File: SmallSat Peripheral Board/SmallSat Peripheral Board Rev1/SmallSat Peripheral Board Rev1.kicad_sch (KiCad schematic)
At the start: 9 parts

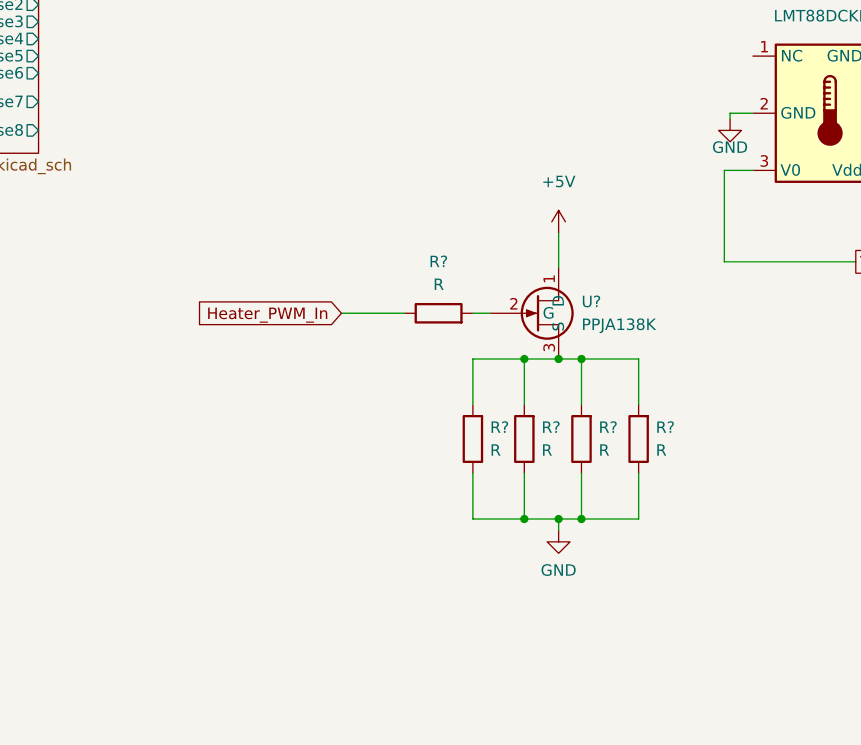
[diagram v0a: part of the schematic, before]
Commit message: Updated Power Section
Now using BQ28Z620DRZR fuel gauge
Now using BQ296202DSGR protection
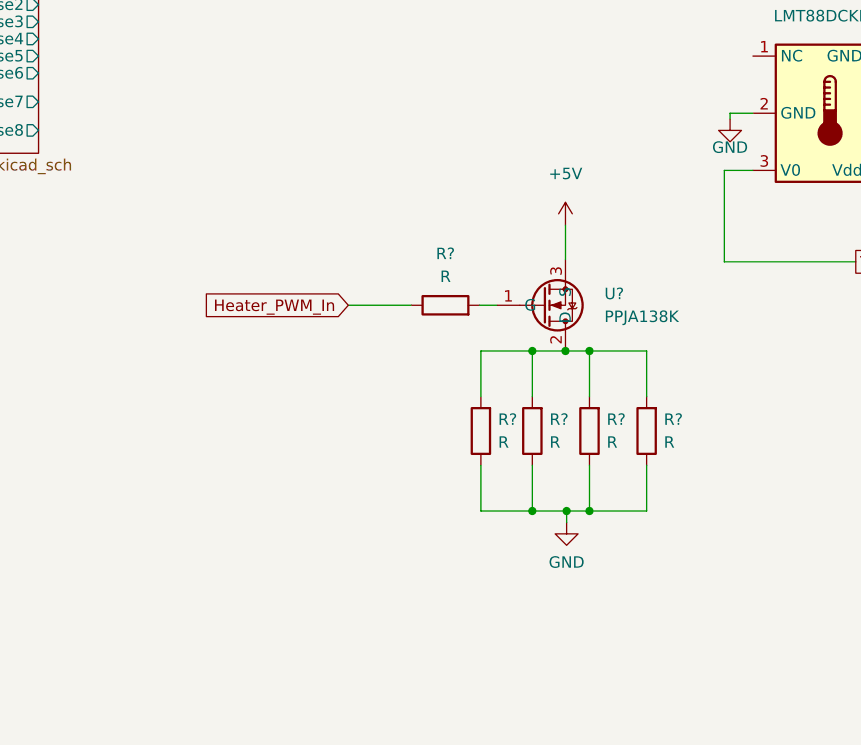
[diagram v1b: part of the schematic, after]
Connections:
- net +5V: now also U?.3 (S); no longer U?.1 (D)
- net at R?.2: now also U?.1 (G); no longer U?.2 (G)
- net at R?.2, R?.2, R?.2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: now also U?.2 (D); no longer U?.3 (S)
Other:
- moved on the sheet: R?

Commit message: Finished First Try for Power Board
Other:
- sheet Power ports: added 3.3V, 5V, FUEL_SCL, FUEL_SDA; removed none
- moved on the sheet: U?

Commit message: PB-order version
Sent the order in for Rev 1 power board with this version
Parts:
- removed U?: L293D, Package_DIP:DIP-16_W7.62mm, symbol Driver_Motor:L293D
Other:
- moved on the sheet: R?, U?

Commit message: Peripheral Board Rev 1 Complete
Time to test!
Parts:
- removed R? (x5): R, symbol Device:R
- removed U?: PPJA138K, symbol SmallSat-Peripherals-Board:PPJA138K
- removed U?: CSI-Connector, symbol SmallSat-Peripherals-Board:CSI-Connector
- removed U?: LMT88DCKR, symbol SmallSat-Peripherals-Board:LMT88DCKR
- added A1: Arduino_Mega2560_R3_Shield, PCM_arduino-library:Arduino_Mega2560_R3_Shield, symbol arduino-library:Arduino_Mega2560_R3_Shield
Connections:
- net GND: now also A1.GND1 (GND), A1.GND2 (GND), A1.GND3 (GND), A1.GND5 (GND), A1.GND6 (GND)
- new net 3.3V: A1.3V3 (3.3V)
- new net 5V: A1.5V1 (5V), A1.5V3 (5V), A1.5V4 (5V)
- new net A0: A1.A0
- new net A1: A1.A1
- new net A2: A1.A2
- new net A3: A1.A3
- new net A4: A1.A4
- new net A5: A1.A5
- new net A6: A1.A6
- new net A7: A1.A7
- new net A9: A1.A9
- new net D22: A1.D22
- new net D23: A1.D23
- new net D24: A1.D24
- new net D26: A1.D26
- new net D27: A1.D27
- new net D28: A1.D28
- new net D29: A1.D29
- new net D30: A1.D30
- new net D4: A1.D4
- new net D5: A1.D5
- new net D6: A1.D6
- new net D8: A1.D8
- new net SCL1: A1.SCL
- new net SCL2: A1.D21 (D21/SCL)
- new net SDA1: A1.SDA
- new net SDA2: A1.D20 (D20/SDA)
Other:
- removed sheet Power
- removed sheet Sun Sensor Array
- added sheet Peripherals (Peripherals.kicad_sch)
- added sheet Power Board Rev 1 (Power Board Rev 1.kicad_sch)
- sheet ADCS Driver ports: added 7.4V, Control1, Control2, Control3, Phase A Bemf, Phase B Bemf, Phase C Bemf; removed PWM_CTL
- note removed: "Inputs are inputs to the peripheral board"
- company: (none) -> Rose SmallSat
- title: (none) -> Suborbital Peripheral Board

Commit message: ADCS Driver Work
Nothing final yet
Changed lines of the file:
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@@
     (effects (font (size 1.27 1.27)) (justify left bottom))
   )
-  (label "D5" (at 215.265 100.457 180) (fields_autoplaced)
+  (label "D6" (at 215.265 100.457 180) (fields_autoplaced)
     (effects (font (size 1.27 1.27)) (justify right bottom))
   )
@@
     (effects (font (size 1.27 1.27)) (justify left bottom))
   )
-  (label "D6" (at 215.265 96.647 180) (fields_autoplaced)
+  (label "D5" (at 215.265 96.647 180) (fields_autoplaced)
     (effects (font (size 1.27 1.27)) (justify right bottom))
   )

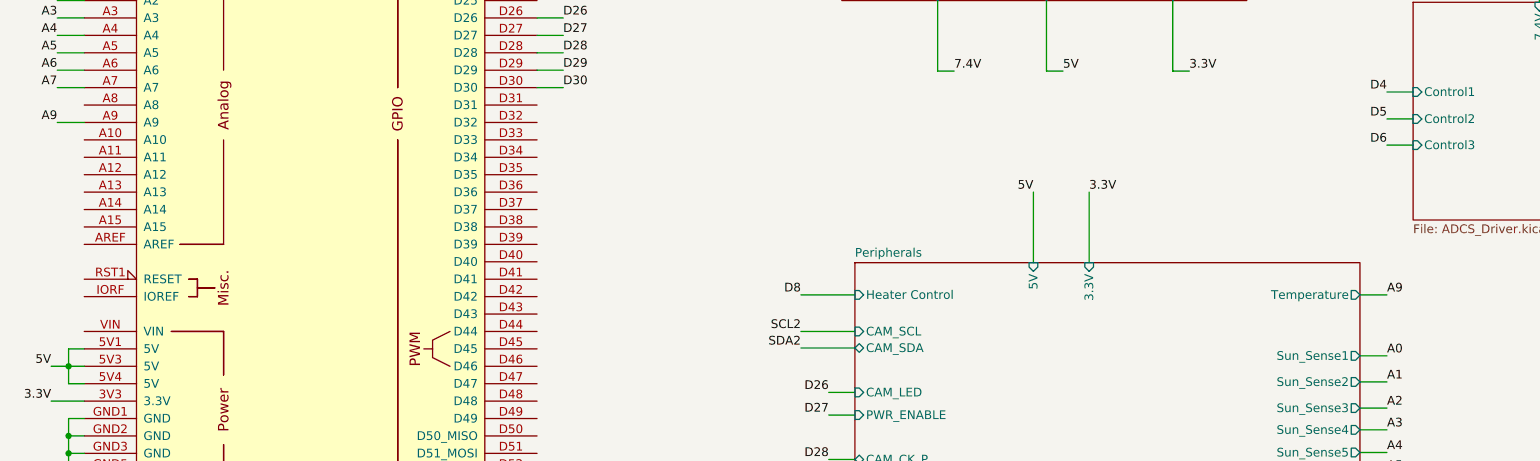
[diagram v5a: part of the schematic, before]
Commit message: ADCS Driver Rev 2
- Redesigned the ESC with modern ICs that have bootstrapping infrastructure
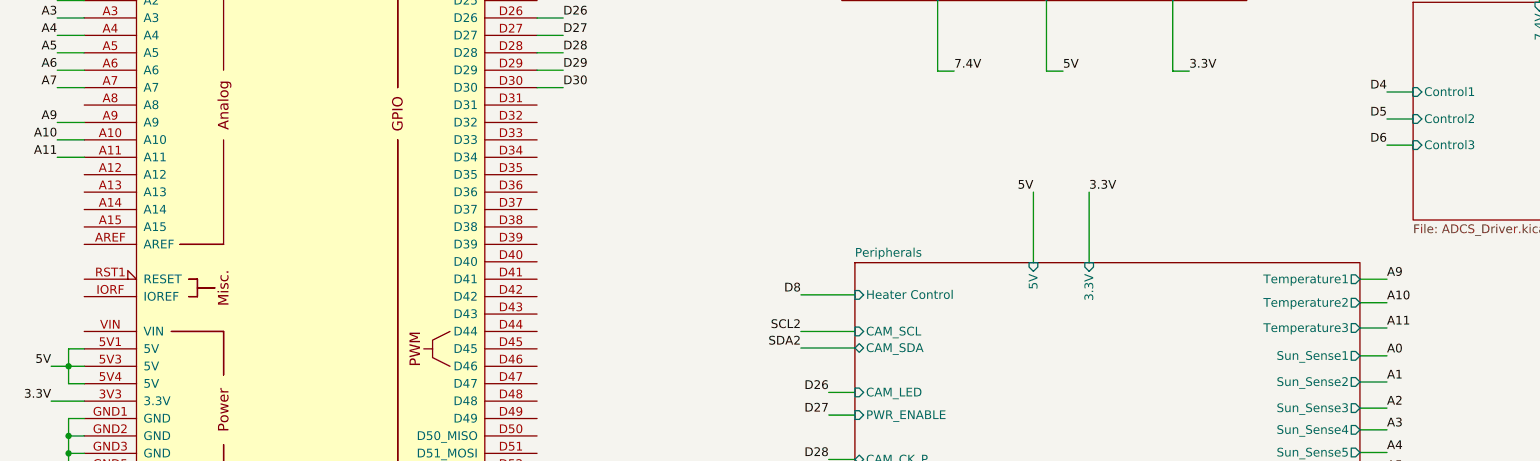
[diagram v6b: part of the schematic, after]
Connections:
- net A10: now reaches A1.A10
- net A11: now reaches A1.A11
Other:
- sheet Peripherals ports: added Temperature1, Temperature2, Temperature3; removed Temperature
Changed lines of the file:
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@@
+    (stroke (width 0) (type default))
+  )
+  (wire (pts (xy 21.336 99.695) (xy 25.273 99.695))
     (stroke (width 0) (type default))
   )
@@
     (stroke (width 0) (type default))
   )
+  (wire (pts (xy 215.265 127.127) (xy 211.328 127.127))
+    (stroke (width 0) (type default))
+  )
   (wire (pts (xy 129.794 122.301) (xy 137.668 122.301))
     (stroke (width 0) (type default))
@@
     (stroke (width 0) (type default))
   )
-  (wire (pts (xy 215.265 122.301) (xy 211.328 122.301))
+  (wire (pts (xy 215.265 120.015) (xy 211.328 120.015))
     (stroke (width 0) (type default))
   )
@@
     (stroke (width 0) (type default))
   )
+  (wire (pts (xy 215.265 123.444) (xy 211.328 123.444))
+    (stroke (width 0) (type default))
+  )
   (wire (pts (xy 21.336 64.135) (xy 25.273 64.135))
     (stroke (width 0) (type default))
@@
     (stroke (width 0) (type default))
   )
+  (wire (pts (xy 21.336 102.235) (xy 25.273 102.235))
+    (stroke (width 0) (type default))
+  )
   (wire (pts (xy 127.889 46.99) (xy 135.763 46.99))
     (stroke (width 0) (type default))
@@
     (effects (font (size 1.27 1.27)) (justify right bottom))
   )
+  (label "A11" (at 21.336 102.235 180) (fields_autoplaced)
+    (effects (font (size 1.27 1.27)) (justify right bottom))
+  )
   (label "3.3V" (at 171.831 107.315 0) (fields_autoplaced)
     (effects (font (size 1.27 1.27)) (justify left bottom))
@@
     (effects (font (size 1.27 1.27)) (justify right bottom))
   )
-  (label "A9" (at 215.265 122.301 0) (fields_autoplaced)
-    (effects (font (size 1.27 1.27)) (justify left bottom))
-  )
   (label "SDA1" (at 21.336 66.675 180) (fields_autoplaced)
     (effects (font (size 1.27 1.27)) (justify right bottom))
@@
     (effects (font (size 1.27 1.27)) (justify right bottom))
   )
+  (label "A10" (at 21.336 99.695 180) (fields_autoplaced)
+    (effects (font (size 1.27 1.27)) (justify right bottom))
+  )
+  (label "A9" (at 215.265 120.015 0) (fields_autoplaced)
+    (effects (font (size 1.27 1.27)) (justify left bottom))
+  )
   (label "D29" (at 133.858 149.86 180) (fields_autoplaced)
     (effects (font (size 1.27 1.27)) (justify right bottom))
@@
     (effects (font (size 1.27 1.27)) (justify left bottom))
   )
+  (label "A11" (at 215.265 127.127 0) (fields_autoplaced)
+    (effects (font (size 1.27 1.27)) (justify left bottom))
+  )
   (label "A4" (at 215.265 145.288 0) (fields_autoplaced)
+    (effects (font (size 1.27 1.27)) (justify left bottom))
+  )
+  (label "A10" (at 215.265 123.444 0) (fields_autoplaced)
     (effects (font (size 1.27 1.27)) (justify left bottom))
   )
@@
       (effects (font (size 1.27 1.27)) (justify right))
     )
-    (pin "Temperature" output (at 211.328 122.301 0)
-      (effects (font (size 1.27 1.27)) (justify right))
-    )
     (pin "Sun_Sense7" output (at 211.328 151.765 0)
       (effects (font (size 1.27 1.27)) (justify right))
@@
       (effects (font (size 1.27 1.27)) (justify left))
     )
+    (pin "Temperature1" output (at 211.328 120.015 0)
+      (effects (font (size 1.27 1.27)) (justify right))
+    )
+    (pin "Temperature2" output (at 211.328 123.444 0)
+      (effects (font (size 1.27 1.27)) (justify right))
+    )
+    (pin "Temperature3" output (at 211.328 127.127 0)
+      (effects (font (size 1.27 1.27)) (justify right))
+    )
     (instances

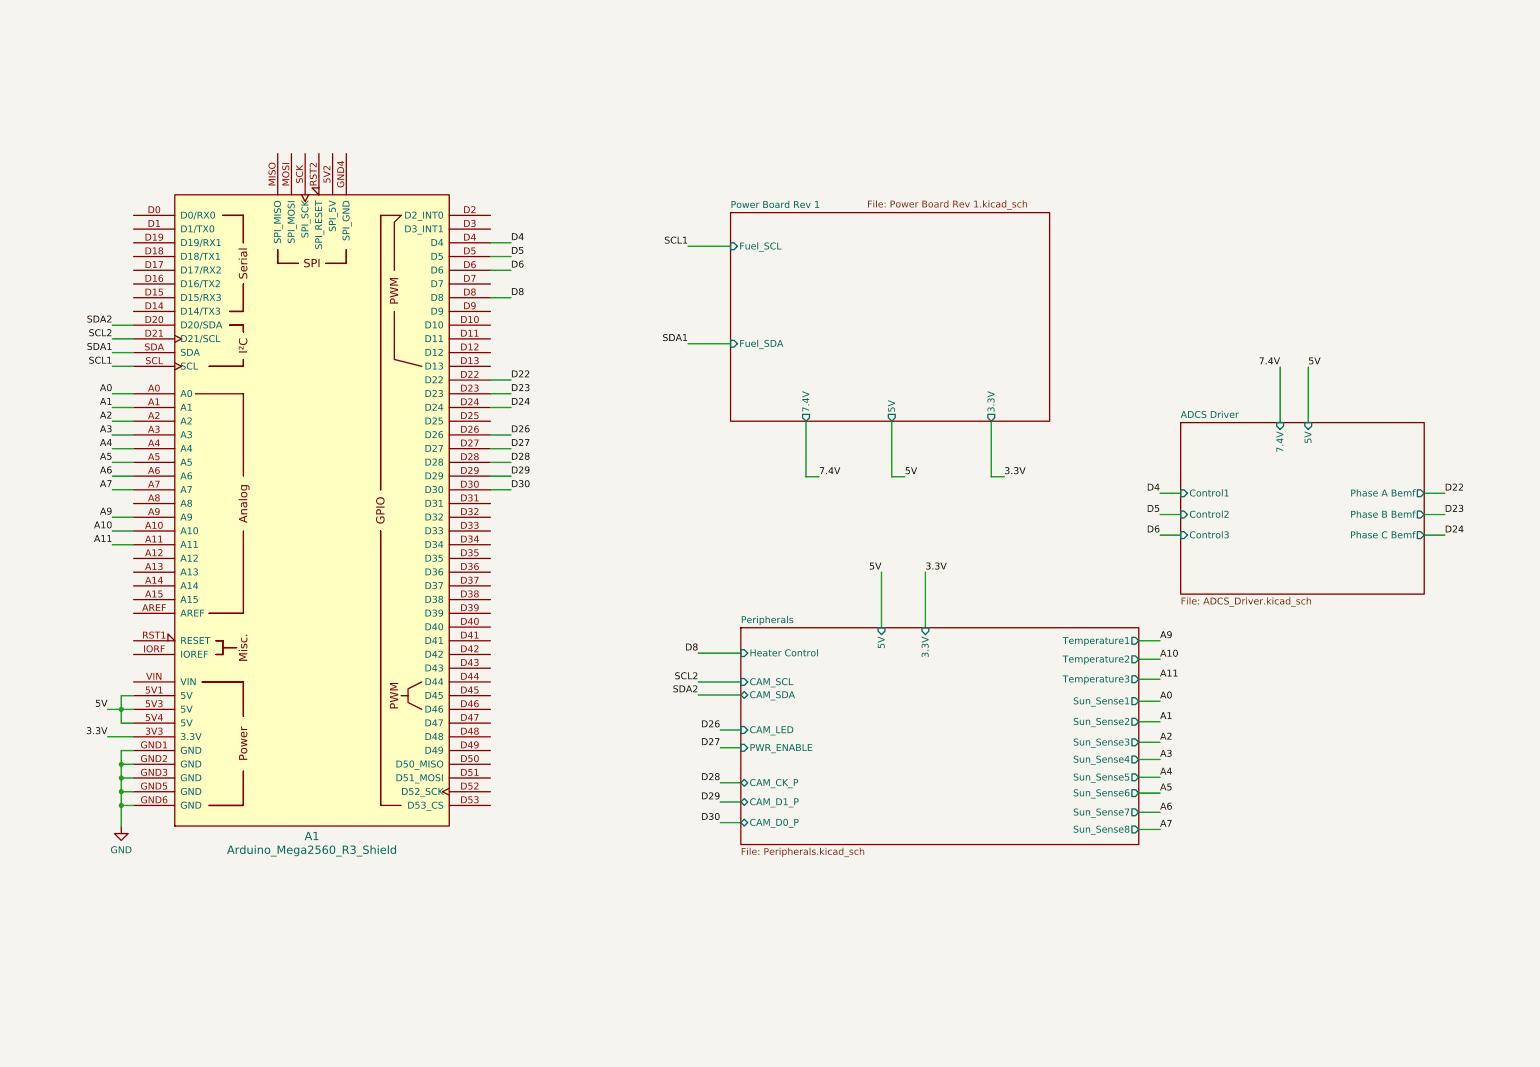
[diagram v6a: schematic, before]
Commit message: Organized Repository
- Better overall file organization
- Included necessary documentation to be filled out
- Included KiCAD libraries
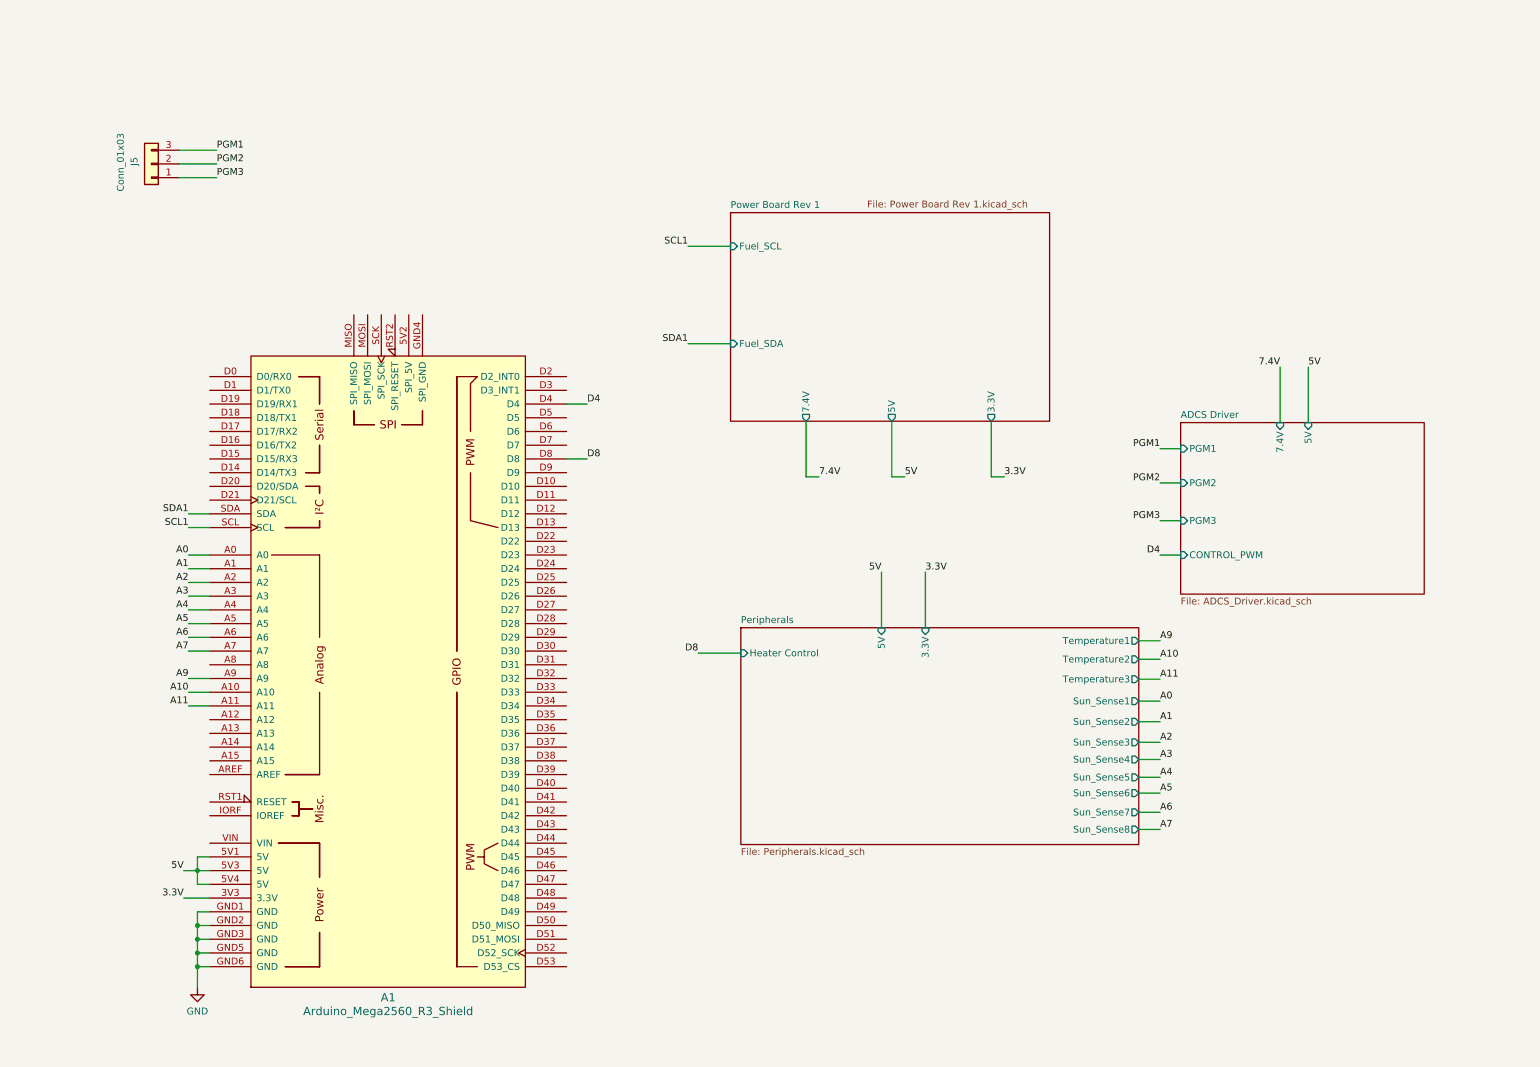
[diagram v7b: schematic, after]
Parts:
- added J5: Conn_01x03, symbol Connector_Generic:Conn_01x03
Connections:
- net D22: no longer names the net of A1.D22
- net D23: no longer names the net of A1.D23
- net D24: no longer names the net of A1.D24
- net D26: no longer names the net of A1.D26
- net D27: no longer names the net of A1.D27
- net D28: no longer names the net of A1.D28
- net D29: no longer names the net of A1.D29
- net D30: no longer names the net of A1.D30
- net D5: no longer names the net of A1.D5
- net D6: no longer names the net of A1.D6
- net SCL2: no longer names the net of A1.D21 (D21/SCL)
- net SDA2: no longer names the net of A1.D20 (D20/SDA)
- new net PGM1: J5.3 (Pin_3)
- new net PGM2: J5.2 (Pin_2)
- new net PGM3: J5.1 (Pin_1)
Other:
- sheet ADCS Driver ports: added CONTROL_PWM, PGM1, PGM2, PGM3; removed Control1, Control2, Control3, Phase A Bemf, Phase B Bemf, Phase C Bemf
- sheet Peripherals ports: added none; removed CAM_CK_P, CAM_D0_P, CAM_D1_P, CAM_LED, CAM_SCL, CAM_SDA, PWR_ENABLE
- moved on the sheet: A1
